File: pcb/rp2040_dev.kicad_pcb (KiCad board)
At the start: 2 copper layers, 94.6 x 64.6 mm, 154 parts, among them J1 USB4105-GF-A, J2 USB4105-GF-A, J3 Micro_SD_Card_Det1, J4 Conn_01x05, J5 10029449-111RLF, J6 USB1035-GF-P-0-B-B, J7 USB1035-GF-P-0-B-B, J8 HR911105A, Q1 SI2300DS, SW1 SW_SPST_3x4mm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

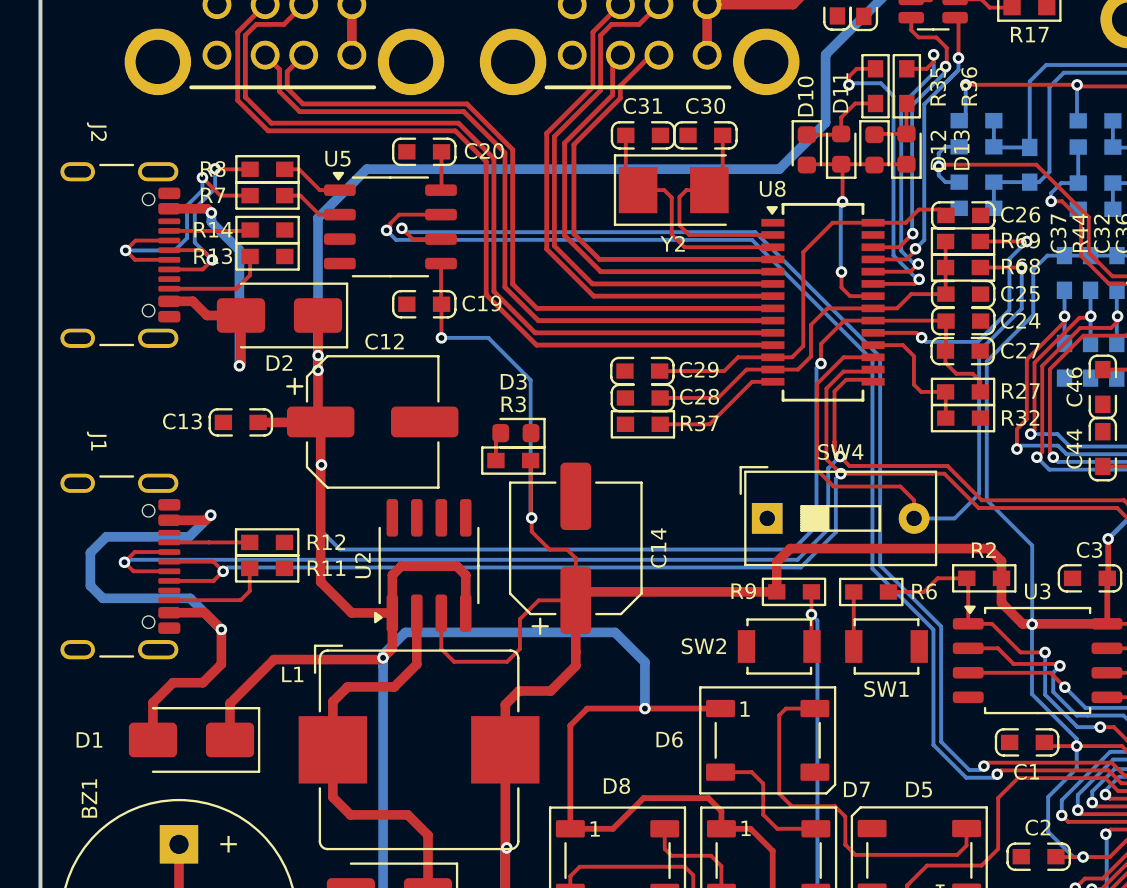
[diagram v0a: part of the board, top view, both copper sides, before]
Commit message: Fix UART0 reversed pins
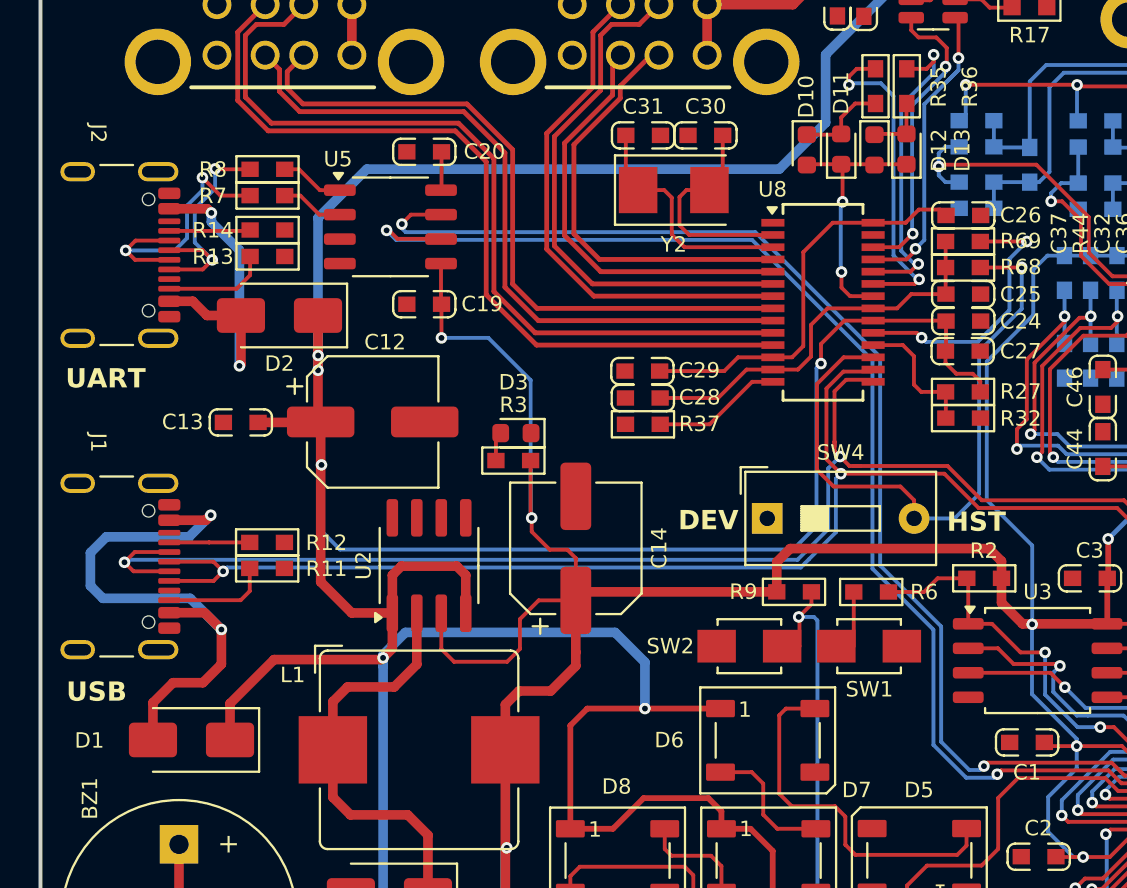
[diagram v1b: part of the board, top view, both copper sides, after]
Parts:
- BZ1: value SBZ-9032 -> Buzzer
- J5: value 10029449-111RLF -> 2000-1-1-20-00-BK
- moved SW2 1.55 mm to (143.7, 113.3)
- moved SW1 0.91 mm to (149.9, 113.3)
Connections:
- U5 pad 6: /UART0_TX -> /UART0_RX
- U5 pad 7: /UART0_RX -> /UART0_TX
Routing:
- net /RESET: track 89.8 -> 91.6 mm
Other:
- board text added: "DEV"
- board text added: "HST"
- board text added: "UART"
- board text added: "USB"
